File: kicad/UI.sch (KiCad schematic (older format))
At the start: 15 parts, among them Q14 DMN3065LW-7, SW2 UPLOAD, U8 PCA9632

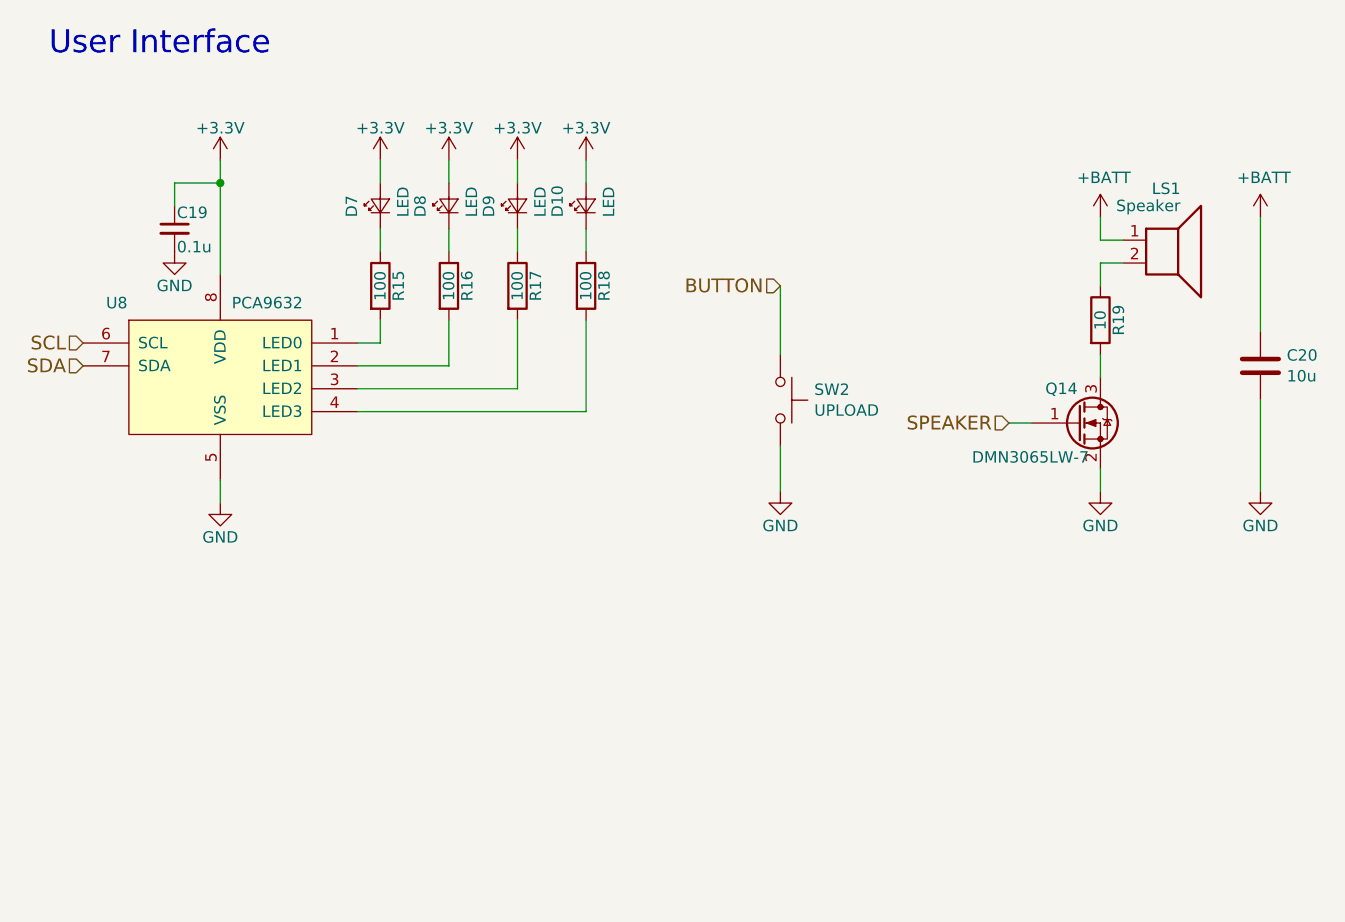
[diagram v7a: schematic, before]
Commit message: 部品を配置
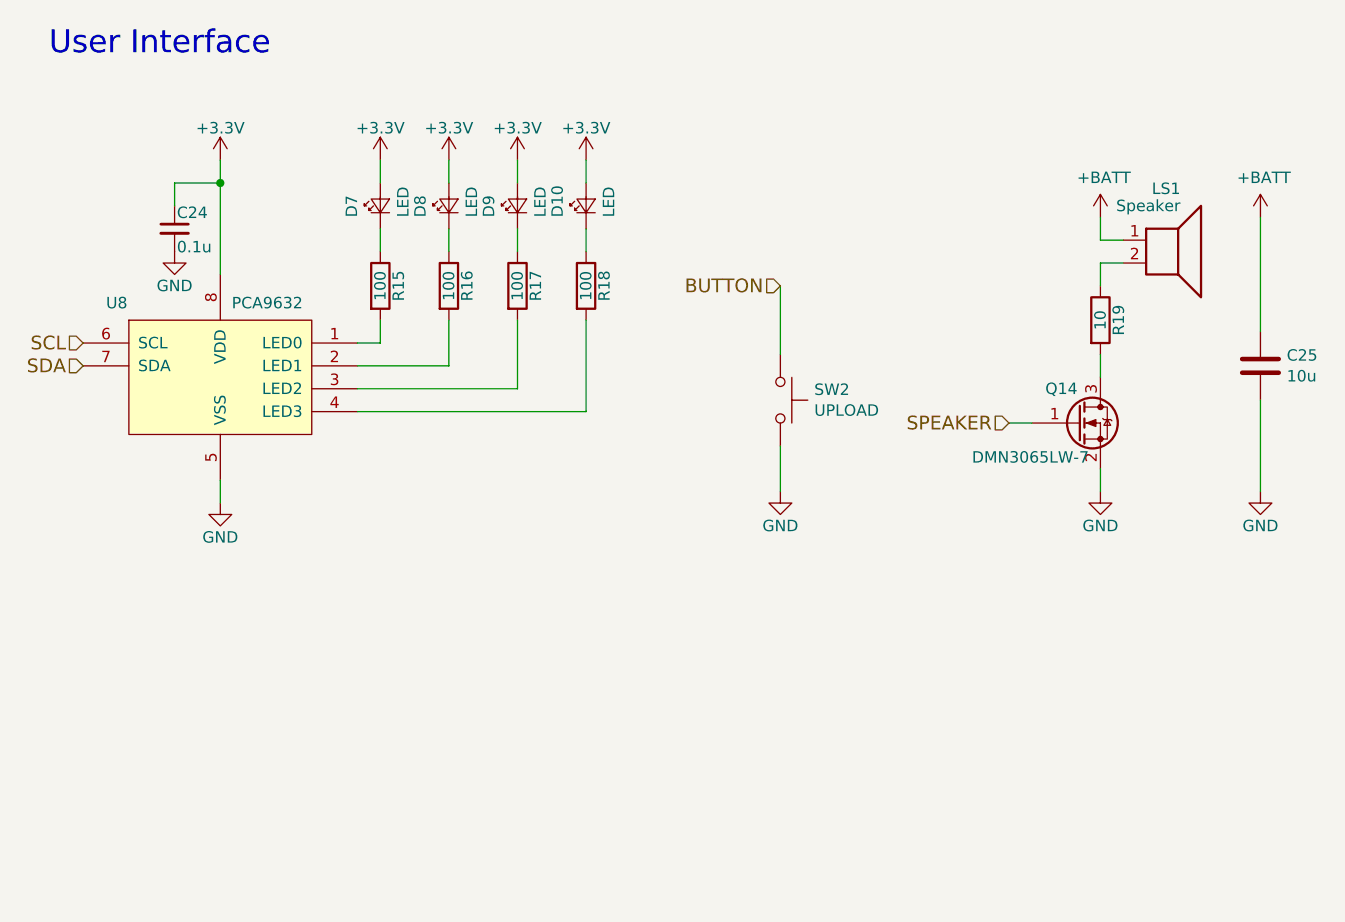
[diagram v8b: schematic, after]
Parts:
- renumbered C19 to C24, C20 to C25
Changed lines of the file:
@@
 $EndDescr
 $Comp
-L power:GND #PWR076
+L power:GND #PWR078
 U 1 1 57CEA2EF
 P 6500 4600
-F 0 "#PWR076" H 6500 4350 50  0001 C CNN
+F 0 "#PWR078" H 6500 4350 50  0001 C CNN
 F 1 "GND" H 6500 4450 50  0000 C CNN
 F 2 "" H 6500 4600 50  0000 C CNN
@@
 	6500 4600 6500 4400
 $Comp
-L power:GND #PWR078
+L power:GND #PWR080
 U 1 1 5A1C53C4
 P 7900 4600
-F 0 "#PWR078" H 7900 4350 50  0001 C CNN
+F 0 "#PWR080" H 7900 4350 50  0001 C CNN
 F 1 "GND" H 7900 4450 50  0000 C CNN
 F 2 "" H 7900 4600 50  0000 C CNN
@@
 SDA
 $Comp
-L power:+3.3V #PWR070
+L power:+3.3V #PWR072
 U 1 1 5A202D5A
 P 4050 3150
-F 0 "#PWR070" H 4050 3000 50  0001 C CNN
+F 0 "#PWR072" H 4050 3000 50  0001 C CNN
 F 1 "+3.3V" H 4050 3290 50  0000 C CNN
 F 2 "" H 4050 3150 50  0001 C CNN
@@
 	4050 3150 4050 3250
 $Comp
-L power:GND #PWR071
+L power:GND #PWR073
 U 1 1 5A202F53
 P 4050 4650
-F 0 "#PWR071" H 4050 4400 50  0001 C CNN
+F 0 "#PWR073" H 4050 4400 50  0001 C CNN
 F 1 "GND" H 4050 4500 50  0000 C CNN
 F 2 "" H 4050 4650 50  0000 C CNN
@@
 	5050 3450 5050 3550
 $Comp
-L power:+3.3V #PWR073
+L power:+3.3V #PWR075
 U 1 1 5A204571
 P 5050 3150
-F 0 "#PWR073" H 5050 3000 50  0001 C CNN
+F 0 "#PWR075" H 5050 3000 50  0001 C CNN
 F 1 "+3.3V" H 5050 3290 50  0000 C CNN
 F 2 "" H 5050 3150 50  0001 C CNN
@@
 	4750 3450 4750 3550
 $Comp
-L power:+3.3V #PWR072
+L power:+3.3V #PWR074
 U 1 1 5A203D72
 P 4750 3150
-F 0 "#PWR072" H 4750 3000 50  0001 C CNN
+F 0 "#PWR074" H 4750 3000 50  0001 C CNN
 F 1 "+3.3V" H 4750 3290 50  0000 C CNN
 F 2 "" H 4750 3150 50  0001 C CNN
@@
 	5650 3450 5650 3550
 $Comp
-L power:+3.3V #PWR075
+L power:+3.3V #PWR077
 U 1 1 5A20460C
 P 5650 3150
-F 0 "#PWR075" H 5650 3000 50  0001 C CNN
+F 0 "#PWR077" H 5650 3000 50  0001 C CNN
 F 1 "+3.3V" H 5650 3290 50  0000 C CNN
 F 2 "" H 5650 3150 50  0001 C CNN
@@
 	5350 3450 5350 3550
 $Comp
-L power:+3.3V #PWR074
+L power:+3.3V #PWR076
 U 1 1 5A204620
 P 5350 3150
-F 0 "#PWR074" H 5350 3000 50  0001 C CNN
+F 0 "#PWR076" H 5350 3000 50  0001 C CNN
 F 1 "+3.3V" H 5350 3290 50  0000 C CNN
 F 2 "" H 5350 3150 50  0001 C CNN
@@
 	5650 4250 5650 3850
 $Comp
-L Device:C_Small C19
+L Device:C_Small C24
 U 1 1 5A2A1F42
 P 3850 3450
-F 0 "C19" H 3860 3520 50  0000 L CNN
+F 0 "C24" H 3860 3520 50  0000 L CNN
 F 1 "0.1u" H 3860 3370 50  0000 L CNN
 F 2 "Capacitor_SMD:C_0201_0603Metric" H 3850 3450 50  0001 C CNN
@@
 $EndComp
 $Comp
-L power:GND #PWR069
+L power:GND #PWR071
 U 1 1 5A2A2041
 P 3850 3550
-F 0 "#PWR069" H 3850 3300 50  0001 C CNN
+F 0 "#PWR071" H 3850 3300 50  0001 C CNN
 F 1 "GND" H 3850 3400 50  0000 C CNN
 F 2 "" H 3850 3550 50  0001 C CNN
@@
 $EndComp
 $Comp
-L power:+BATT #PWR077
+L power:+BATT #PWR079
 U 1 1 5C29DB6A
 P 7900 3400
-F 0 "#PWR077" H 7900 3250 50  0001 C CNN
+F 0 "#PWR079" H 7900 3250 50  0001 C CNN
 F 1 "+BATT" H 7915 3573 50  0000 C CNN
 F 2 "" H 7900 3400 50  0001 C CNN
@@
 $EndComp
 $Comp
-L Device:C C20
+L Device:C C25
 U 1 1 5C29E0A6
 P 8600 4050
-F 0 "C20" H 8715 4096 50  0000 L CNN
+F 0 "C25" H 8715 4096 50  0000 L CNN
 F 1 "10u" H 8715 4005 50  0000 L CNN
 F 2 "Capacitor_SMD:C_0402_1005Metric" H 8638 3900 50  0001 C CNN
@@
 $EndComp
 $Comp
-L power:+BATT #PWR079
+L power:+BATT #PWR081
 U 1 1 5C29E17B
 P 8600 3400
-F 0 "#PWR079" H 8600 3250 50  0001 C CNN
+F 0 "#PWR081" H 8600 3250 50  0001 C CNN
 F 1 "+BATT" H 8615 3573 50  0000 C CNN
 F 2 "" H 8600 3400 50  0001 C CNN
@@
 $EndComp
 $Comp
-L power:GND #PWR080
+L power:GND #PWR082
 U 1 1 5C29E1A4
 P 8600 4600
-F 0 "#PWR080" H 8600 4350 50  0001 C CNN
+F 0 "#PWR082" H 8600 4350 50  0001 C CNN
 F 1 "GND" H 8600 4450 50  0000 C CNN
 F 2 "" H 8600 4600 50  0000 C CNN
